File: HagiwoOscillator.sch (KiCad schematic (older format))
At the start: 5 parts

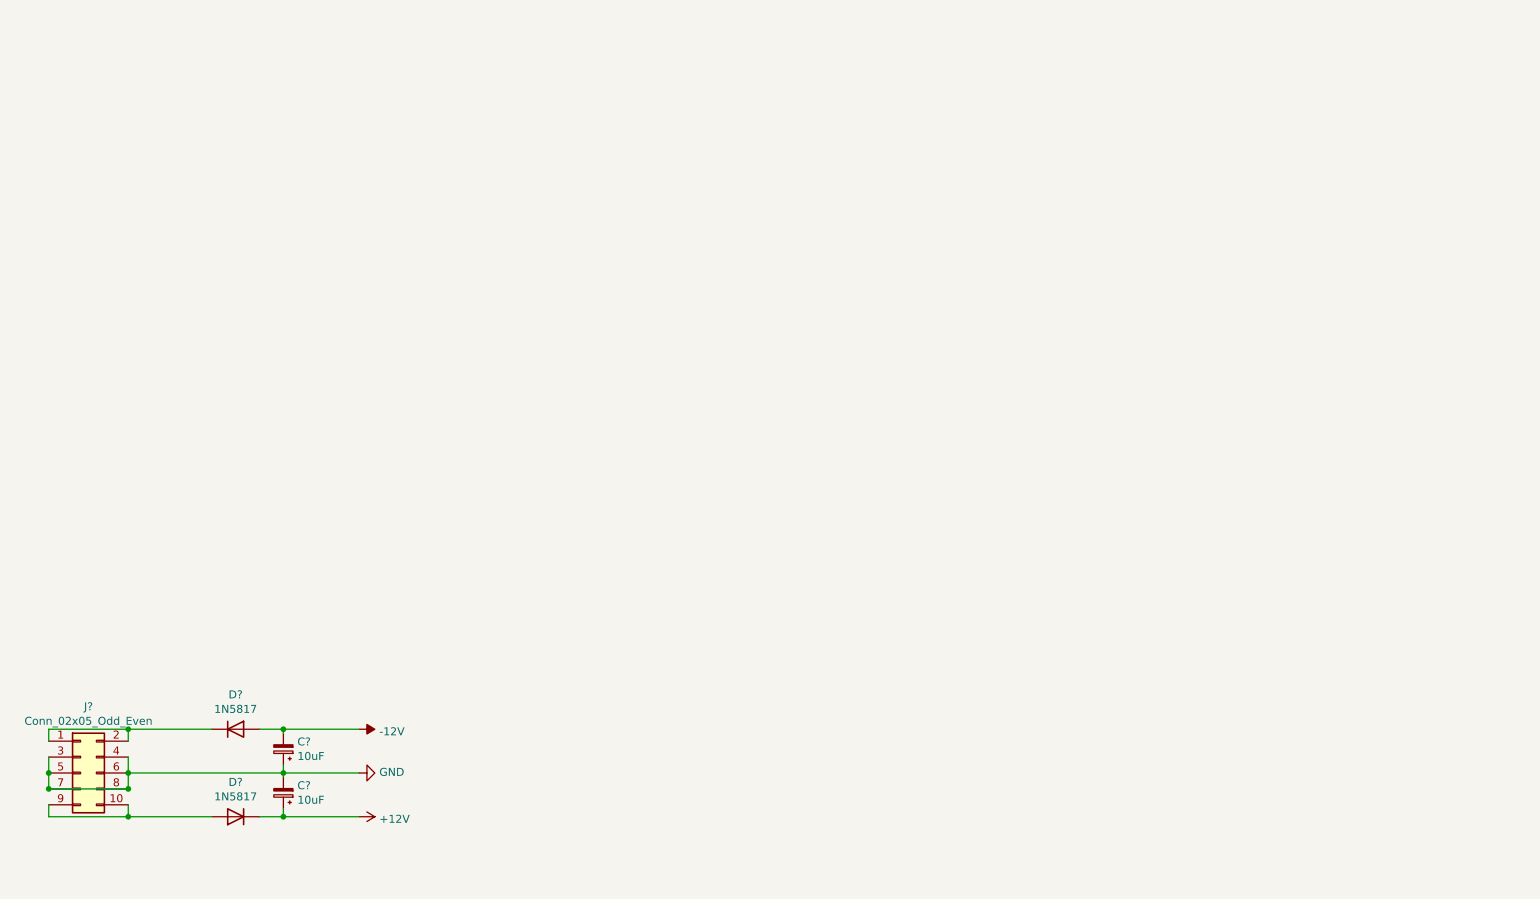
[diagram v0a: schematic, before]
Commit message: 1voct input
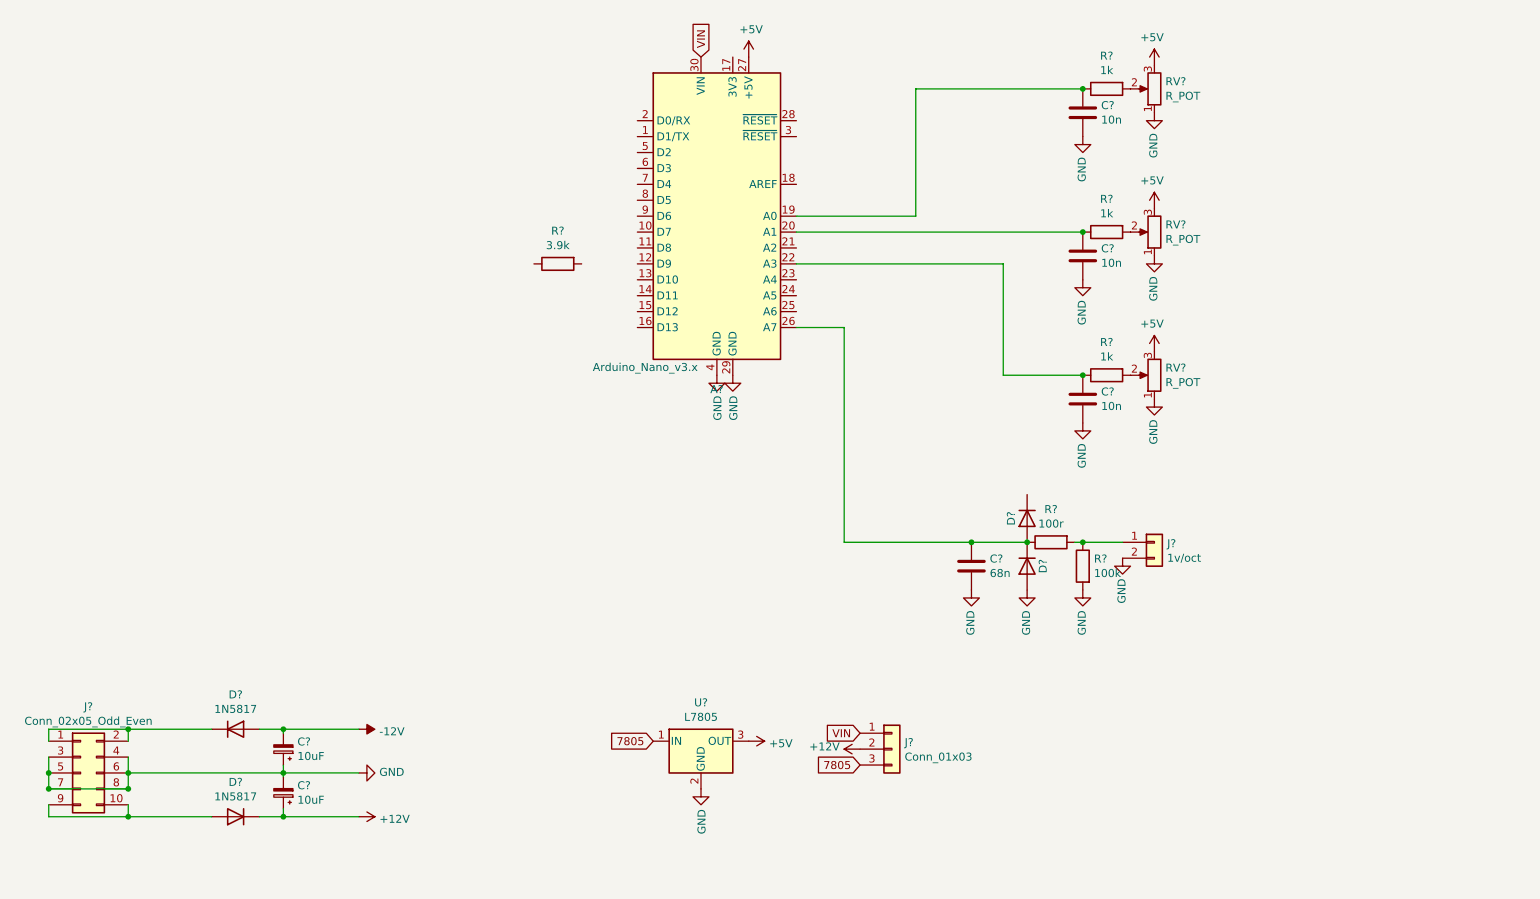
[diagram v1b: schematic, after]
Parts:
- added A?: Arduino_Nano_v3.x, Module:Arduino_Nano, symbol MCU_Module:Arduino_Nano_v3.x
- added C? (x3): 10n, symbol Device:C
- added C?: 68n, symbol Device:C
- added D? (x2): 1N5817, Sonosus:Diode_DO-35, symbol Device:D
- added J?: Conn_01x03, symbol Connector_Generic:Conn_01x03
- added J?: 1v/oct, symbol Connector_Generic:Conn_01x02
- added R? (x3): 1k, symbol Device:R
- added R?: 100r, symbol Device:R
- added R?: 100k, symbol Device:R
- added R?: 3.9k, symbol Device:R
- added RV? (x3): R_POT, symbol Device:R_POT
- added U?: L7805, symbol Regulator_Linear:L7805
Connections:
- net +12V: now also J?.2 (Pin_2)
- net GND: now also A?.29 (GND), A?.4 (GND), C?.2, C?.2, C?.2, C?.2, D?.2 (A), J?.2 (Pin_2), R?.2, RV?.1, RV?.1, RV?.1, U?.2 (GND)
- new net: A?.19 (A0), C?.1, R?.1
- new net: A?.20 (A1), C?.1, R?.1
- new net: A?.22 (A3), C?.1, R?.1
- new net: A?.26 (A7), C?.1, D?.1 (K), D?.2 (A), R?.1
- new net: R?.2, RV?.2 (x3)
- new net: J?.1 (Pin_1), R?.1, R?.2
- new net +5V: A?.27 (+5V), RV?.3, RV?.3, RV?.3, U?.3 (OUT)
- new net 7805: J?.3 (Pin_3), U?.1 (IN)
- new net VIN: A?.30 (VIN), J?.1 (Pin_1)

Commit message: finish schem
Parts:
- added C? (x2): 10n, symbol Device:C
- added C?: 4.7u, symbol Device:C
- added C? (x2): 68n, symbol Device:C
- added C? (x2): 100n, symbol Device:C
- added D? (x6): 1N5817, Sonosus:Diode_DO-35, symbol Device:D
- added J?: out, symbol Connector_Generic:Conn_01x02
- added J? (x2): in1, symbol Connector_Generic:Conn_01x02
- added R?: 510k, symbol Device:R
- added R?: 3.9k, symbol Device:R
- added R?: 220r, symbol Device:R
- added R? (x2): 1k, symbol Device:R
- added R? (x2): 100k, symbol Device:R
- added U? (x3): TL072, symbol Amplifier_Operational:TL072
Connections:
- net +12V: now also C?.2, U?.8 (V+)
- net +5V: now also D?.1 (K), D?.1 (K), D?.1 (K), D?.1 (K)
- net -12V: now also C?.2, U?.4 (V-)
- net GND: now also C?.1, C?.1, C?.2, C?.2, C?.2, C?.2, D?.2 (A), D?.2 (A), D?.2 (A), J?.2 (Pin_2), J?.2 (Pin_2), J?.2 (Pin_2), R?.2, R?.2, U?.5 (+)
- net at A?.12 (D9): now also R?.2
- net at A?.13 (D10): now also R?.2
- net at A?.23 (A4): now also C?.1, D?.1 (K), D?.2 (A), R?.1, R?.1
- net at A?.24 (A5): now also C?.1, D?.1 (K), D?.2 (A), R?.1, R?.1
- net at R?.1: now also C?.1, R?.1, R?.2
- new net: C?.1, R?.1, U?.3 (+)
- new net: R?.2, U?.1, U?.2 (-)
- new net: U?.6 (-), U?.7
- new net: C?.1, D?.1 (K), D?.2 (A), R?.1
- new net: C?.2, J?.1 (Pin_1)
- new net: J?.1 (Pin_1), R?.2 (x2)
- no-connect marks 0 -> 15
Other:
- moved on the sheet: C?, D?, J?, R?

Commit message: footprints
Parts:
- C1, C10, C11, C12, C13, C4, C5, C6, C7, C8, C9: renamed from C?; footprint (none) -> Sonosus:Capacitor_NonPolarized
- J2, J4, J5, J6: renamed from J?; footprint (none) -> Connector_PinHeader_2.54mm:PinHeader_1x02_P2.54mm_Vertical
- J3: renamed from J?; footprint (none) -> Connector_PinHeader_2.54mm:PinHeader_1x03_P2.54mm_Vertical
- R1, R10, R11, R12, R13, R2, R3, R4, R5, R6, R7, R8, R9: renamed from R?; footprint (none) -> Sonosus:Resistor
- RV1, RV2, RV3: renamed from RV?; footprint (none) -> Sonosus:Potentiometer_Alpha_RD901F-40-00D_centred
- U1: renamed from U?; footprint (none) -> Sonosus:DIP-8_Socket
- U2: renamed from U?; footprint (none) -> Sonosus:Regulator_TO-220-3
- gave numbers to parts that had none: 14
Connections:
- no-connect marks 15 -> 18

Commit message: remove rs and cs by pots
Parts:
- removed C10, C11, C9: 10n, Sonosus:Capacitor_NonPolarized, symbol Device:C
- removed R7, R8, R9: 1k, Sonosus:Resistor, symbol Device:R
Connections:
- net at A1.19 (A0): now also RV1.2
- net at A1.20 (A1): now also RV2.2
- net at A1.22 (A3): now also RV3.2
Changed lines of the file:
@@
-$EndComp
-$Comp
-L Device:R R7
-U 1 1 60E0E94B
-P 8200 2550
-F 0 "R7" V 7993 2550 50  0000 C CNN
-F 1 "1k" V 8084 2550 50  0000 C CNN
-F 2 "Sonosus:Resistor" V 8130 2550 50  0001 C CNN
-F 3 "~" H 8200 2550 50  0001 C CNN
-	1    8200 2550
-	0    -1   1    0
 $EndComp
 $Comp
@@
 $EndComp
 $Comp
-L Device:R R8
-U 1 1 60E13B9F
-P 8200 3450
-F 0 "R8" V 7993 3450 50  0000 C CNN
-F 1 "1k" V 8084 3450 50  0000 C CNN
-F 2 "Sonosus:Resistor" V 8130 3450 50  0001 C CNN
-F 3 "~" H 8200 3450 50  0001 C CNN
-	1    8200 3450
-	0    -1   1    0
-$EndComp
-$Comp
 L Device:R_POT RV2
 U 1 1 60E13BA9
@@
 $EndComp
 $Comp
-L Device:C C9
-U 1 1 60E1BADE
-P 8050 2700
-F 0 "C9" H 8165 2746 50  0000 L CNN
-F 1 "10n" H 8165 2655 50  0000 L CNN
-F 2 "Sonosus:Capacitor_NonPolarized" H 8088 2550 50  0001 C CNN
-F 3 "~" H 8050 2700 50  0001 C CNN
-	1    8050 2700
-	1    0    0    -1
-$EndComp
-$Comp
-L power:GND #PWR023
-U 1 1 60E1C0DB
-P 8050 2850
-F 0 "#PWR023" H 8050 2600 50  0001 C CNN
-F 1 "GND" V 8055 2722 50  0000 R CNN
-F 2 "" H 8050 2850 50  0001 C CNN
-F 3 "" H 8050 2850 50  0001 C CNN
-	1    8050 2850
-	-1   0    0    -1
-$EndComp
-$Comp
-L Device:C C10
-U 1 1 60E1C2E8
-P 8050 3600
-F 0 "C10" H 8165 3646 50  0000 L CNN
-F 1 "10n" H 8165 3555 50  0000 L CNN
-F 2 "Sonosus:Capacitor_NonPolarized" H 8088 3450 50  0001 C CNN
-F 3 "~" H 8050 3600 50  0001 C CNN
-	1    8050 3600
-	1    0    0    -1
-$EndComp
-$Comp
-L power:GND #PWR024
-U 1 1 60E1C7E6
-P 8050 3750
-F 0 "#PWR024" H 8050 3500 50  0001 C CNN
-F 1 "GND" V 8055 3622 50  0000 R CNN
-F 2 "" H 8050 3750 50  0001 C CNN
-F 3 "" H 8050 3750 50  0001 C CNN
-	1    8050 3750
-	-1   0    0    -1
-$EndComp
-$Comp
 L power:GND #PWR033
 U 1 1 60E1CBE1
@@
 	1    8500 4200
 	-1   0    0    -1
-$EndComp
-$Comp
-L Device:R R9
-U 1 1 60E1CE45
-P 8200 4350
-F 0 "R9" V 7993 4350 50  0000 C CNN
-F 1 "1k" V 8084 4350 50  0000 C CNN
-F 2 "Sonosus:Resistor" V 8130 4350 50  0001 C CNN
-F 3 "~" H 8200 4350 50  0001 C CNN
-	1    8200 4350
-	0    -1   1    0
 $EndComp
 $Comp
@@
 	-1   0    0    1
 $EndComp
-$Comp
-L Device:C C11
-U 1 1 60E1CE59
-P 8050 4500
-F 0 "C11" H 8165 4546 50  0000 L CNN
-F 1 "10n" H 8165 4455 50  0000 L CNN
-F 2 "Sonosus:Capacitor_NonPolarized" H 8088 4350 50  0001 C CNN
-F 3 "~" H 8050 4500 50  0001 C CNN
-	1    8050 4500
-	1    0    0    -1
-$EndComp
-$Comp
-L power:GND #PWR025
-U 1 1 60E1CE63
-P 8050 4650
-F 0 "#PWR025" H 8050 4400 50  0001 C CNN
-F 1 "GND" V 8055 4522 50  0000 R CNN
-F 2 "" H 8050 4650 50  0001 C CNN
-F 3 "" H 8050 4650 50  0001 C CNN
-	1    8050 4650
-	-1   0    0    -1
-$EndComp
-Wire Wire Line
-	8050 2550 7000 2550
 Wire Wire Line
 	7000 2550 7000 3350
 Wire Wire Line
 	7000 3350 6250 3350
-Connection ~ 8050 2550
-Wire Wire Line
-	8050 3450 6250 3450
-Connection ~ 8050 3450
-Wire Wire Line
-	8050 4350 7550 4350
 Wire Wire Line
 	7550 4350 7550 3650
 Wire Wire Line
 	7550 3650 6250 3650
-Connection ~ 8050 4350
 $Comp
 L Connector_Generic:Conn_01x02 J4
@@
 Wire Wire Line
 	3450 6850 3500 6850
+Wire Wire Line
+	7000 2550 8350 2550
+Wire Wire Line
+	6250 3450 8350 3450
+Wire Wire Line
+	7550 4350 8350 4350
 $EndSCHEMATC
